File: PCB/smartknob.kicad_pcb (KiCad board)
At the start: 2 copper layers, 61.9 x 61.9 mm, 3 parts, among them SW1 RotaryEncoder_Switch_MP, SW2 SW_SP3T, U1 XIAO-ESP32-S3-DIP

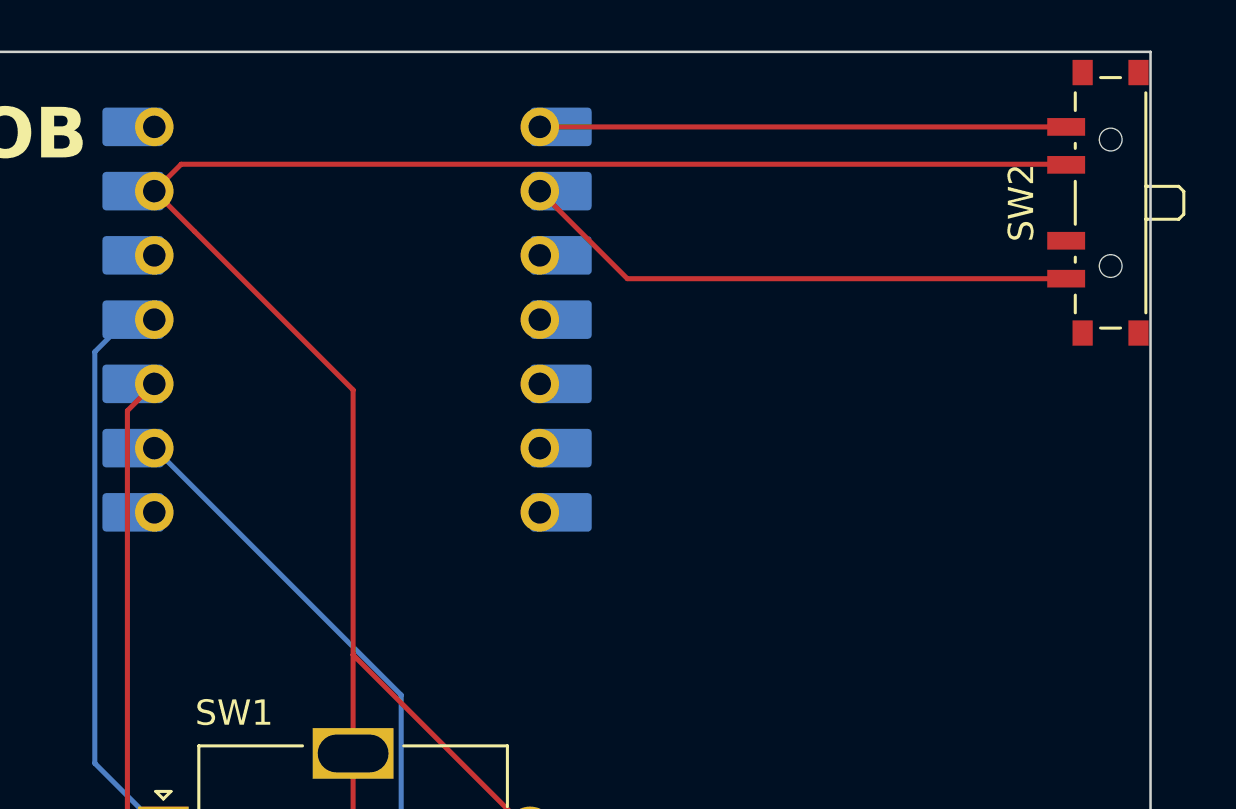
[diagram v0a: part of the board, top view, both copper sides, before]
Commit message: Fixed PCB design rules
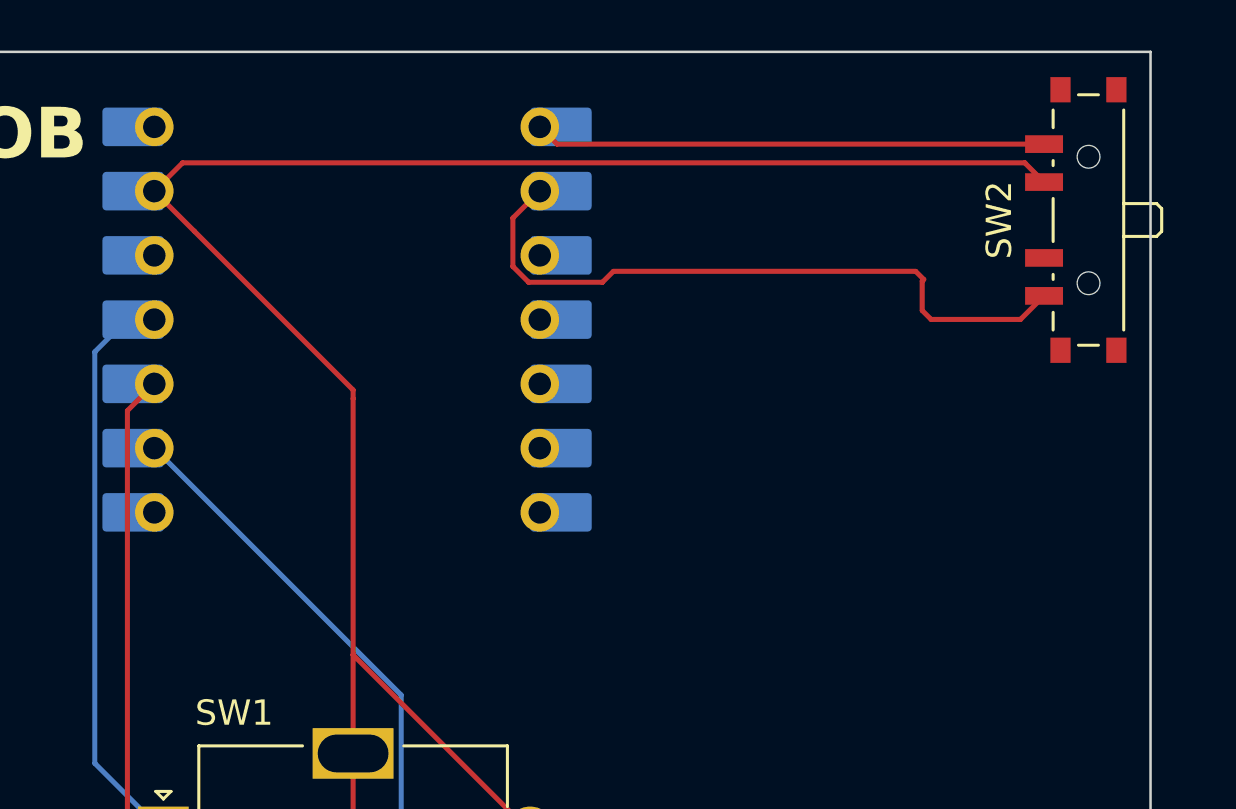
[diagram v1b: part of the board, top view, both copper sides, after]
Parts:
- moved SW2 1.11 mm to (140.1, 68.6)
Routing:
- net Net-(U1-GPIO2/DA/A1): track 22.2 -> 26.8 mm
- net Net-(U1-GPIO1/D0/A0): track 20.8 -> 20.2 mm
- net GND: track 90.6 -> 90.1 mm
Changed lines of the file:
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@@
 	(footprint "Button_Switch_SMD:SW_SP3T_PCM13"
 		(layer "F.Cu")
-		(at 140.97 67.88 90)
+		(at 140.095 68.56 90)
 		(descr "Ultraminiature Surface Mount Slide Switch, right-angle, https://www.ckswitches.com/media/1424/pcm.pdf")
 		(property "Reference" "SW2"
@@
 	(segment
 		(start 111.350027 85.75)
+		(end 111.350027 75.62)
+		(width 0.2)
+		(layer "F.Cu")
+		(net 3)
+	)
+	(segment
+		(start 111.350027 75.62)
 		(end 111.350027 75.278527)
+		(width 0.2)
+		(layer "F.Cu")
+		(net 3)
+	)
+	(segment
+		(start 138.665 67.06)
+		(end 137.905 66.3)
 		(width 0.2)
 		(layer "F.Cu")
@@
 	)
 	(segment
-		(start 139.5155 66.3555)
-		(end 104.553 66.3555)
-		(width 0.2)
-		(layer "F.Cu")
-		(net 3)
-	)
-	(segment
 		(start 111.350027 75.278527)
 		(end 105.07575 69.00425)
@@
 	)
 	(segment
+		(start 104.6085 66.3)
+		(end 103.49 67.4185)
+		(width 0.2)
+		(layer "F.Cu")
+		(net 3)
+	)
+	(segment
 		(start 105.07575 69.00425)
 		(end 103.49 67.4185)
@@
 	)
 	(segment
-		(start 104.553 66.3555)
-		(end 103.49 67.4185)
-		(width 0.2)
-		(layer "F.Cu")
-		(net 3)
-	)
-	(segment
 		(start 111.350027 95.21)
 		(end 111.350027 89.65)
@@
 	)
 	(segment
-		(start 139.54 66.38)
-		(end 139.5155 66.3555)
+		(start 137.905 66.3)
+		(end 104.6085 66.3)
 		(width 0.2)
 		(layer "F.Cu")
@@
 	)
 	(segment
-		(start 139.54 64.88)
-		(end 118.7315 64.88)
+		(start 119.4115 65.56)
+		(end 118.73 64.8785)
 		(width 0.2)
 		(layer "F.Cu")
@@
 	)
 	(segment
-		(start 118.7315 64.88)
-		(end 118.73 64.8785)
+		(start 138.665 65.56)
+		(end 119.4115 65.56)
 		(width 0.2)
 		(layer "F.Cu")
@@
 	)
 	(segment
-		(start 122.1915 70.88)
+		(start 138.665 71.56)
+		(end 137.734 72.491)
+		(width 0.2)
+		(layer "F.Cu")
+		(net 14)
+	)
+	(segment
+		(start 133.849 72.138943)
+		(end 133.849 70.971)
+		(width 0.2)
+		(layer "F.Cu")
+		(net 14)
+	)
+	(segment
+		(start 118.28969 71.0215)
+		(end 117.667 70.39881)
+		(width 0.2)
+		(layer "F.Cu")
+		(net 14)
+	)
+	(segment
+		(start 117.667 70.39881)
+		(end 117.667 68.4815)
+		(width 0.2)
+		(layer "F.Cu")
+		(net 14)
+	)
+	(segment
+		(start 133.91 70.91)
+		(end 133.59 70.59)
+		(width 0.2)
+		(layer "F.Cu")
+		(net 14)
+	)
+	(segment
+		(start 133.849 70.971)
+		(end 133.91 70.91)
+		(width 0.2)
+		(layer "F.Cu")
+		(net 14)
+	)
+	(segment
+		(start 121.64 70.59)
+		(end 121.2085 71.0215)
+		(width 0.2)
+		(layer "F.Cu")
+		(net 14)
+	)
+	(segment
+		(start 121.2085 71.0215)
+		(end 118.28969 71.0215)
+		(width 0.2)
+		(layer "F.Cu")
+		(net 14)
+	)
+	(segment
+		(start 133.59 70.59)
+		(end 121.64 70.59)
+		(width 0.2)
+		(layer "F.Cu")
+		(net 14)
+	)
+	(segment
+		(start 134.201057 72.491)
+		(end 133.849 72.138943)
+		(width 0.2)
+		(layer "F.Cu")
+		(net 14)
+	)
+	(segment
+		(start 137.734 72.491)
+		(end 134.201057 72.491)
+		(width 0.2)
+		(layer "F.Cu")
+		(net 14)
+	)
+	(segment
+		(start 117.667 68.4815)
 		(end 118.73 67.4185)
 		(width 0.2)
 		(layer "F.Cu")
-		(net 14)
-	)
-	(segment
-		(start 139.54 70.88)
-		(end 122.1915 70.88)
-		(width 0.2)
-		(layer "F.Cu")
